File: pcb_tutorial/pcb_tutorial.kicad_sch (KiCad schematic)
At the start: 0 parts

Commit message: Adding components
Adding some of the components
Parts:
- added C?: 1uF, symbol Device:C_Small
- added R? (x2): 22, symbol Device:R_Small
- added R? (x2): 10k, symbol Device:R_Small
- added SW1: SW_Push, symbol Switch:SW_Push
- added U1: ATmega32U4-A, Package_QFP:TQFP-44_10x10mm_P0.8mm, symbol MCU_Microchip_ATmega:ATmega32U4-A
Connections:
- new net: C?.1, U1.6 (UCAP)
- new net: R?.2, U1.4 (D+)
- new net: R?.2, SW1.2, U1.13 (~{RESET})
- new net: R?.1, U1.33 (~{HWB}/PE2)
- new net: R?.2, U1.3 (D-)
- new net +5V: R?.1, U1.14 (VCC), U1.2 (UVCC), U1.24 (AVCC), U1.34 (VCC), U1.44 (AVCC), U1.7 (VBUS)
- new net D+: R?.1, R?.1
- new net GND: C?.2, R?.2, SW1.1, U1.15 (GND), U1.23 (GND), U1.35 (GND), U1.43 (GND), U1.5 (UGND)

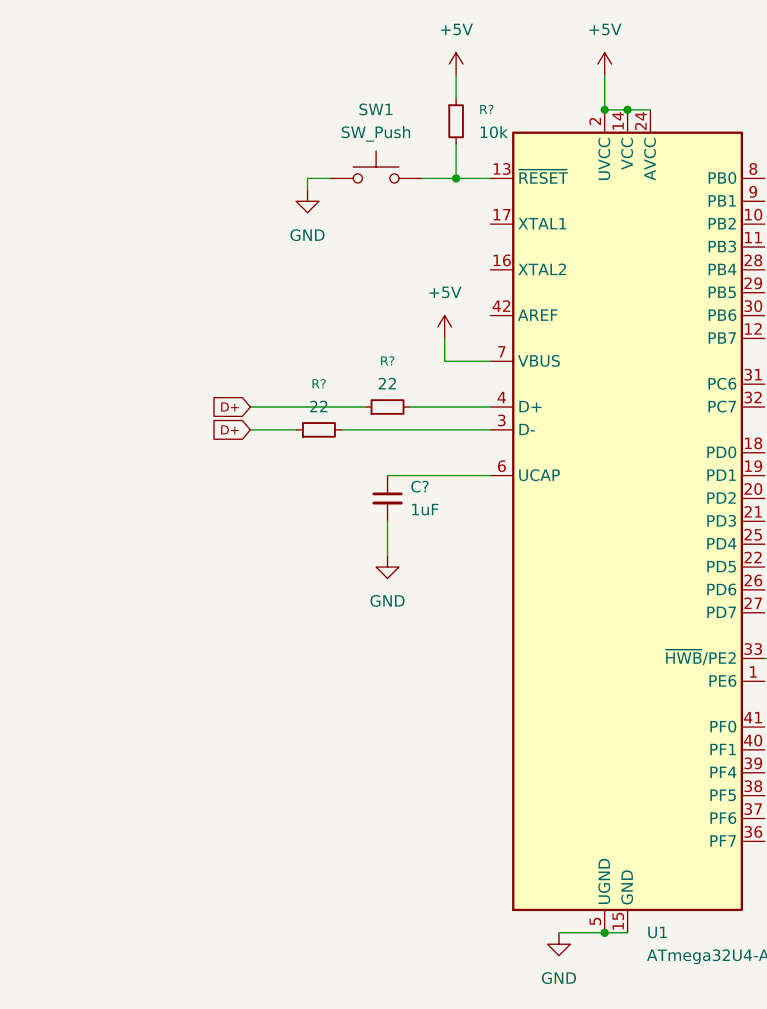
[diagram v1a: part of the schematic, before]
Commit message: usb connector
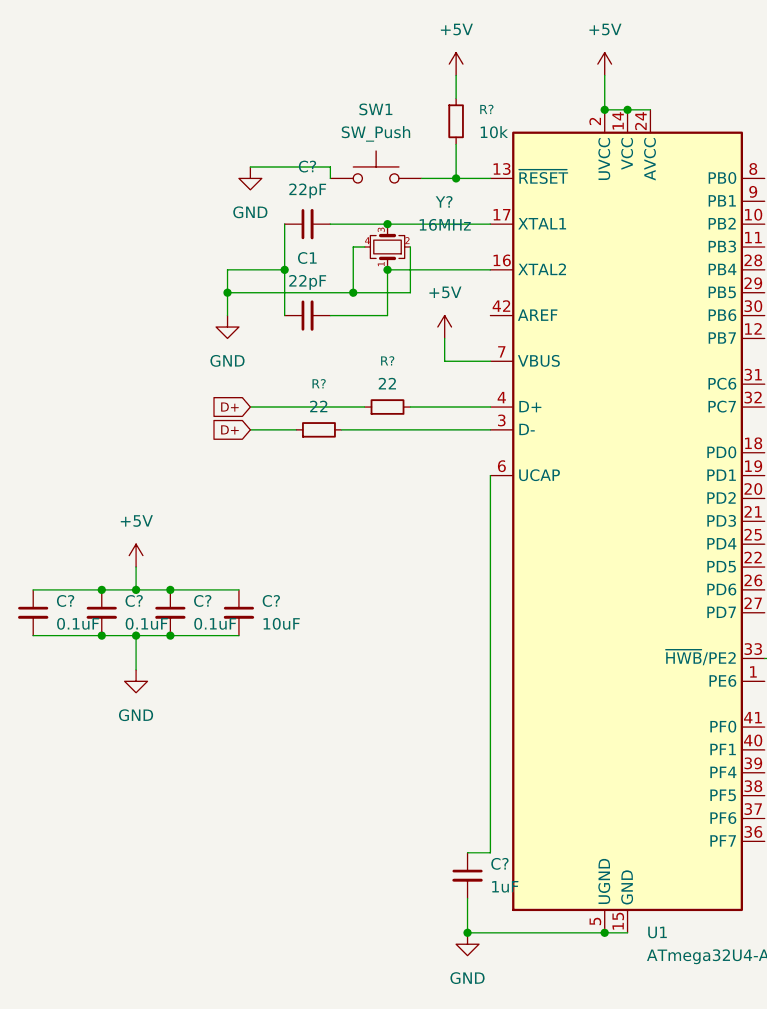
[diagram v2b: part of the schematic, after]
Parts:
- added C1, C?: 22pF, symbol Device:C_Small
- added C? (x3): 0.1uF, symbol Device:C_Small
- added C?: 10uF, symbol Device:C_Small
- added Y?: 16MHz, symbol Device:Crystal_GND24_Small
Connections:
- net +5V: now also C?.1, C?.1, C?.1, C?.1
- net GND: now also C1.1, C?.1, C?.2, C?.2, C?.2, C?.2, Y?.2, Y?.4
- net at U1.16 (XTAL2): now also C1.2, Y?.1
- net at U1.17 (XTAL1): now also C?.2, Y?.3
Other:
- moved on the sheet: C?

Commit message: getting ready everything
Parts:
- added D1, D2, D3, D4: SOD-123, Diode_SMD:D_SOD-123, symbol Device:D_Small
- added F1: 500mA, Fuse:Fuse_1206_3216Metric, symbol Device:Polyfuse_Small
- added MX1, MX2, MX3, MX4: MX-NoLED, MX_Alps_Hybrid:MX-1U-NoLED, symbol MX_Alps_Hybrid:MX-NoLED
- added USB1: Molex-0548190589, random-keyboard-parts:Molex-0548190589, symbol random-keyboard-parts:Molex-0548190589
- C1: footprint (none) -> Capacitor_SMD:C_0805_2012Metric
- C2, C3, C4, C5, C6, C7: renamed from C?; footprint (none) -> Capacitor_SMD:C_0805_2012Metric
- R1, R2, R3, R4: renamed from R?; footprint (none) -> Resistor_SMD:R_0805_2012Metric
- SW1: footprint (none) -> random-keyboard-parts:SKQG-1155865
- Y1: renamed from Y?; footprint (none) -> Crystal:Crystal_SMD_3225-4Pin_3.2x2.5mm
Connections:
- net +5V: now also F1.2
- net D+: now also USB1.3 (D+); no longer R3.1
- net GND: now also USB1.1 (GND)
- new net: D1.2 (A), MX1.2 (ROW)
- new net: D3.2 (A), MX3.2 (ROW)
- new net: D4.2 (A), MX4.2 (ROW)
- new net: D2.2 (A), MX2.2 (ROW)
- new net COL0: MX1.1 (COL), MX3.1 (COL)
- new net COL1: MX2.1 (COL), MX4.1 (COL)
- new net D-: R3.1, USB1.4 (D-)
- new net ROW0: D1.1 (K), D2.1 (K)
- new net ROW1: D3.1 (K), D4.1 (K)
- new net VCC: F1.1, USB1.5 (VBUS)

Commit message: adding more lines
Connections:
- net COL0: now also U1.10 (PB2)
- net COL1: now also U1.9 (PB1)
- net ROW0: now also U1.8 (PB0)
- net ROW1: now also U1.11 (PB3)
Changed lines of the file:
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@@
+		)
+	)
+	(global_label "ROW0"
+		(shape input)
+		(at 156.21 48.26 0)
+		(fields_autoplaced yes)
+		(effects
+			(font
+				(size 1.016 1.016)
+			)
+			(justify left)
+		)
+		(property "Intersheetrefs" "${INTERSHEET_REFS}"
+			(at 162.807 48.26 0)
+			(effects
+				(font
+					(size 1.27 1.27)
+				)
+				(justify left)
+				(hide yes)
+			)
 		)
 	)
@@
 			(effects
 				(font
+					(size 1.27 1.27)
+				)
+				(justify left)
+				(hide yes)
+			)
+		)
+	)
+	(global_label "COL0"
+		(shape input)
+		(at 156.21 53.34 0)
+		(fields_autoplaced yes)
+		(effects
+			(font
+				(size 1.016 1.016)
+			)
+			(justify left)
+		)
+		(property "Intersheetrefs" "${INTERSHEET_REFS}"
+			(at 162.4684 53.34 0)
+			(effects
+				(font
+					(size 1.27 1.27)
+				)
+				(justify left)
+				(hide yes)
+			)
+		)
+	)
+	(global_label "COL1"
+		(shape input)
+		(at 156.21 50.8 0)
+		(fields_autoplaced yes)
+		(effects
+			(font
+				(size 1.016 1.016)
+			)
+			(justify left)
+		)
+		(property "Intersheetrefs" "${INTERSHEET_REFS}"
+			(at 162.4684 50.8 0)
+			(effects
+				(font
+					(size 1.27 1.27)
+				)
+				(justify left)
+				(hide yes)
+			)
+		)
+	)
+	(global_label "ROW1"
+		(shape input)
+		(at 156.21 55.88 0)
+		(fields_autoplaced yes)
+		(effects
+			(font
+				(size 1.016 1.016)
+			)
+			(justify left)
+		)
+		(property "Intersheetrefs" "${INTERSHEET_REFS}"
+			(at 162.807 55.88 0)
+			(effects
+				(font
